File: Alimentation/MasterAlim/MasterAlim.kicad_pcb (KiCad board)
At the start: 4 copper layers, 46.5 x 36.2 mm, 41 parts, among them J1 Ext-Con, J11 AU Logic, J12 INHIBIT, J2 Alim logique, J4 INHIBIT, J6 INHIBIT, J8 INHIBIT, U1 74LVC1G02, U2 74LVC1G02, U3 74LVC1G02, U4 74LVC1G02, U8 PCF8574A

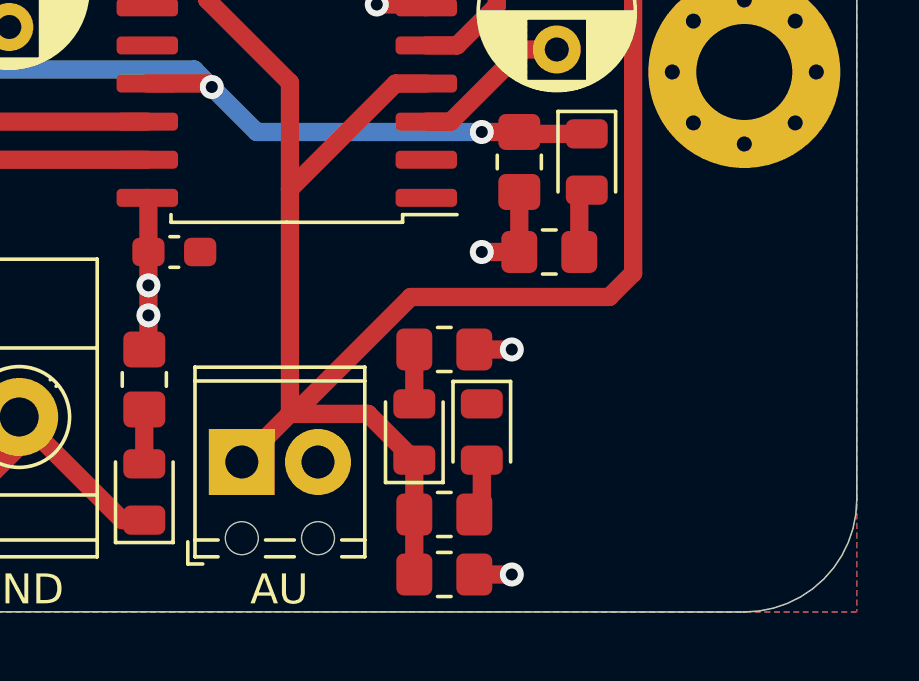
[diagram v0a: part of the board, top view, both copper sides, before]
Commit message: Fix Master Alim : affichage statut AU
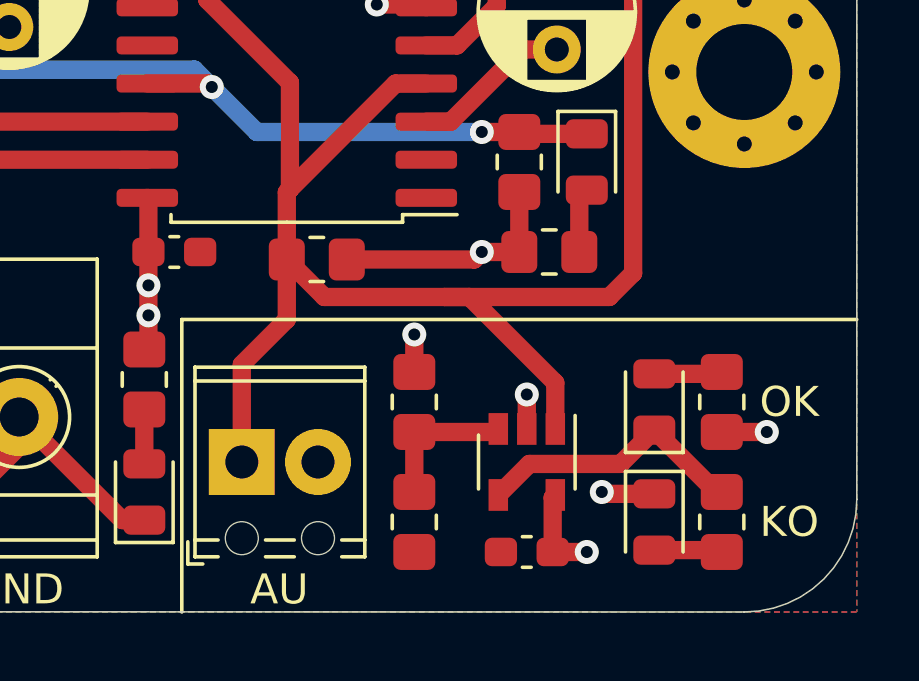
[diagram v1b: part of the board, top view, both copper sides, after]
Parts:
- added C4: 100n, Capacitor_SMD:C_0603_1608Metric_Pad1.08x0.95mm_HandSolder, F.Cu at (131.0, 69.5)
- added R10: 4.7k, Resistor_SMD:R_0805_2012Metric_Pad1.20x1.40mm_HandSolder, F.Cu at (127.2, 68.5)
- added R9: 4.7k, Resistor_SMD:R_0805_2012Metric_Pad1.20x1.40mm_HandSolder, F.Cu at (127.2, 64.5)
- added U5: LM321, Package_TO_SOT_SMD:SOT-23-5, F.Cu at (131.0, 66.5)
- moved R1 11.3 mm to (124.0, 59.8)
- moved R4 9.41 mm to (137.5, 64.5), turned to 90 degrees
- moved R2 9.25 mm to (137.5, 68.5), turned to 270 degrees
- moved D3 8.06 mm to (135.2, 64.5)
- moved D1 6.49 mm to (135.2, 68.5)
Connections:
- D3 pad 1: /AU -> Net-(D3-Pad1)
- R2 pad 1: /AU -> Net-(D3-Pad1)
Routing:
- net Net-(D3-Pad1): track 0.00 -> 9.20 mm
- net +5V: track 48.7 -> 56.7 mm, vias 6 -> 7
- net Net-(R10-Pad1): track 0.00 -> 4.84 mm
- net /AU: track 82.3 -> 79.2 mm
- net GND: track 47.9 -> 50.9 mm, vias 8 -> 10
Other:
- board text added: "KO"
- board text added: "OK"
- board text removed: "JLCJLCJLCJLC"

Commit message: Upgrade alim to Kicad 7
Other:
- net class Default removed
